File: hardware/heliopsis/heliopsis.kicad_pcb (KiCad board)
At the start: 2 copper layers, 70.7 x 53.3 mm, 311 parts, among them J1 NEIGHBOR1, J11 NEIGHBOR1, J12 NEIGHBOR2, J17 BONUS_ROW, J2 NEIGHBOR2, J7 BONUS_ROW, P1101 smd-proto-pad, P11010 smd-proto-pad, P11011 smd-proto-pad, P11012 smd-proto-pad, P11013 smd-proto-pad, P11014 smd-proto-pad, P11015 smd-proto-pad, P1102 smd-proto-pad, P1103 smd-proto-pad, P1104 smd-proto-pad, P1105 smd-proto-pad, P1106 smd-proto-pad, P1107 smd-proto-pad, P1108 smd-proto-pad, P1109 smd-proto-pad, P111 smd-proto-pad, P1110 smd-proto-pad, P1111 smd-proto-pad, P11110 smd-proto-pad, P11111 smd-proto-pad, P11112 smd-proto-pad, P11113 smd-proto-pad, P11114 smd-proto-pad, P11115 smd-proto-pad, P1112 smd-proto-pad, P1113 smd-proto-pad, P1114 smd-proto-pad, P1115 smd-proto-pad, P1116 smd-proto-pad, P1117 smd-proto-pad, P1118 smd-proto-pad, P1119 smd-proto-pad, P112 smd-proto-pad, P1121 smd-proto-pad, P11210 smd-proto-pad, P11211 smd-proto-pad, P11212 smd-proto-pad, P11213 smd-proto-pad, P11214 smd-proto-pad, P11215 smd-proto-pad, P1122 smd-proto-pad, P1123 smd-proto-pad, P1124 smd-proto-pad, P1125 smd-proto-pad, P1126 smd-proto-pad, P1127 smd-proto-pad, P1128 smd-proto-pad, P1129 smd-proto-pad, P113 smd-proto-pad, P1131 smd-proto-pad, P11310 smd-proto-pad, P11311 smd-proto-pad, P11312 smd-proto-pad, P11313 smd-proto-pad, P11314 smd-proto-pad, P11315 smd-proto-pad, P1132 smd-proto-pad, P1133 smd-proto-pad, P1134 smd-proto-pad, P1135 smd-proto-pad, P1136 smd-proto-pad, P1137 smd-proto-pad, P1138 smd-proto-pad, P1139 smd-proto-pad, P114 smd-proto-pad, P1141 smd-proto-pad, P11410 smd-proto-pad, P11411 smd-proto-pad, P11412 smd-proto-pad, P11413 smd-proto-pad, P11414 smd-proto-pad, P11415 smd-proto-pad, P1142 smd-proto-pad, P1143 smd-proto-pad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

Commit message: Update date for this version
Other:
- board text added: "2 September 2016"
- board text removed: "18 August 2016"
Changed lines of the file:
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@@
   (gr_line (start 177.9016 92.3544) (end 177.8508 94.0054) (angle 90) (layer Edge.Cuts) (width 0.15))
   (gr_line (start 177.9524 90.5002) (end 177.9016 92.3544) (angle 90) (layer Edge.Cuts) (width 0.15))
-  (gr_text "18 August 2016" (at 153.416 114.681) (layer F.SilkS)
+  (gr_text "2 September 2016" (at 153.416 114.681) (layer F.SilkS)
     (effects (font (size 0.762 0.5715) (thickness 0.1143)))
   )

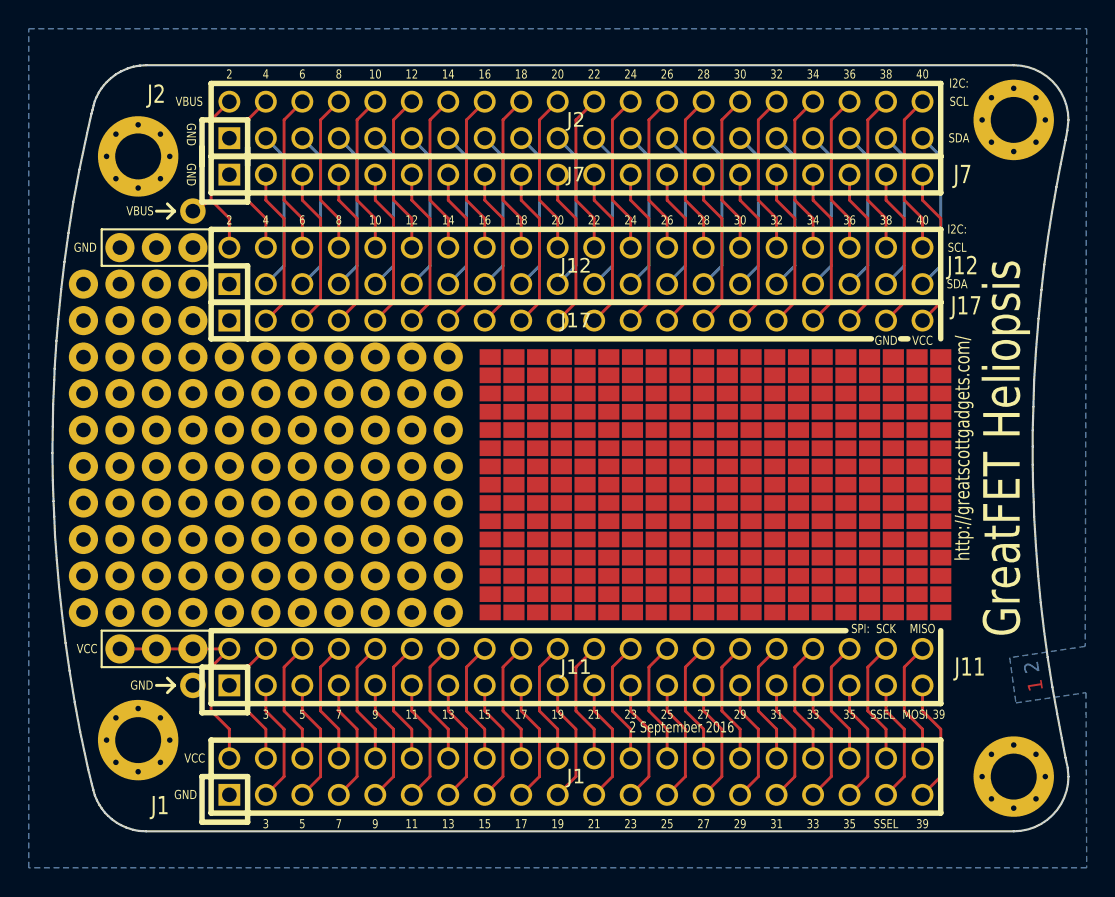
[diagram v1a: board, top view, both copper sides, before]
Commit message: Make power traces wider
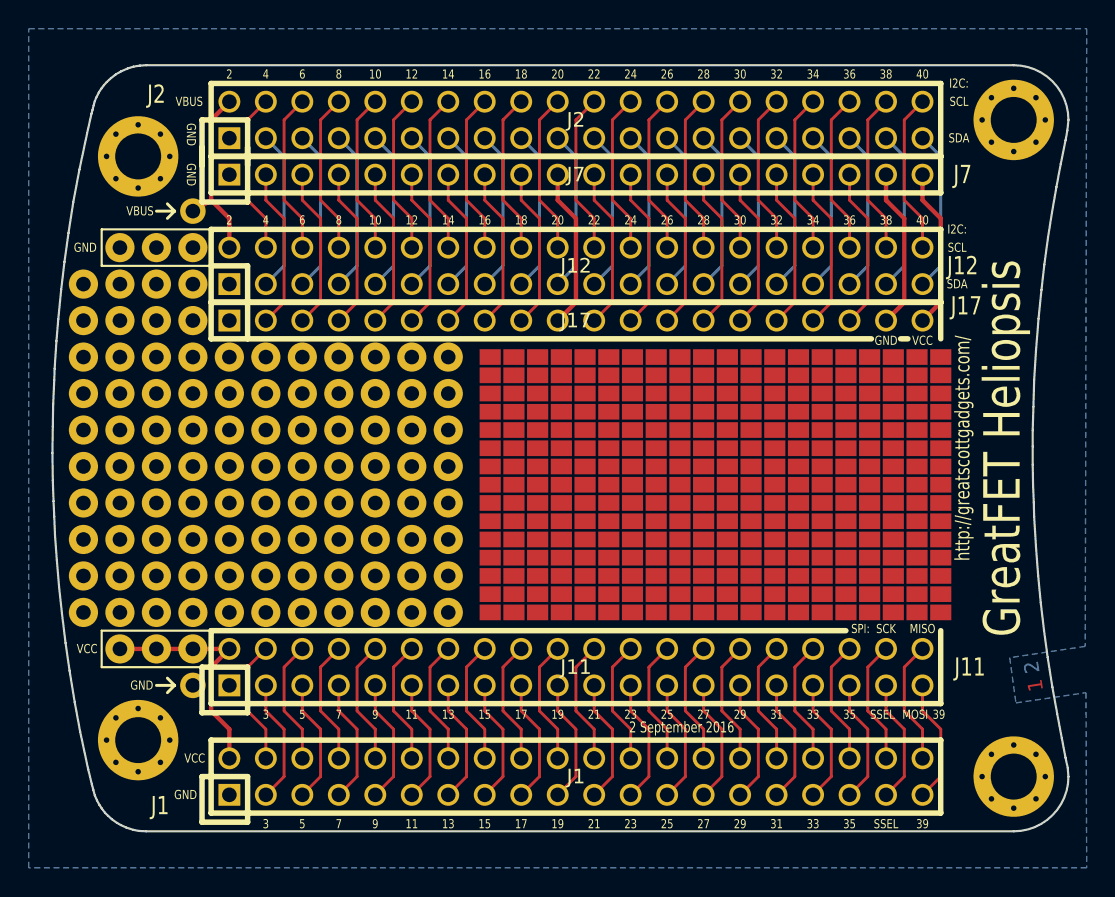
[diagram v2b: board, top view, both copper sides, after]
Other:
- net class Power added: clearance 0.1524, trace_width 0.3048, via_dia 0.762, via_drill 0.3302
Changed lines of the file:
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@@
-(kicad_pcb (version 4) (host pcbnew 4.0.2-stable)
+(kicad_pcb (version 4) (host pcbnew 4.0.4-stable)
   (general
     (links 149)
@@
   )
   (setup
-    (last_trace_width 0.2032)
+    (last_trace_width 0.3048)
     (user_trace_width 0.3048)
     (user_trace_width 0.508)
@@
     (visible_elements FFFFF77F)
     (pcbplotparams
-      (layerselection 0x010e8_80000001)
+      (layerselection 0x010f0_80000001)
       (usegerberextensions false)
       (excludeedgelayer true)
@@
     (add_net /RTC_ALARM)
     (add_net /VBAT)
-    (add_net /VBUS)
     (add_net /WAKEUP0)
+  )
+  (net_class Power ""
+    (clearance 0.1524)
+    (trace_width 0.3048)
+    (via_dia 0.762)
+    (via_drill 0.3302)
+    (uvia_dia 0.508)
+    (uvia_drill 0.2032)
+    (add_net /VBUS)
     (add_net GND)
     (add_net VCC)
@@
   (gr_line (start 176.53 121.92) (end 116.1288 121.92) (angle 90) (layer Edge.Cuts) (width 0.15))
   (gr_line (start 116.1288 68.58) (end 176.53 68.58) (angle 90) (layer Edge.Cuts) (width 0.15))
-  (segment (start 167.64 77.978) (end 167.64 76.2) (width 0.2032) (layer F.Cu) (net 1) (status 20))
-  (segment (start 168.91 79.248) (end 167.64 77.978) (width 0.2032) (layer F.Cu) (net 1))
-  (segment (start 168.91 85.09) (end 168.91 79.248) (width 0.2032) (layer F.Cu) (net 1))
-  (segment (start 167.64 86.36) (end 168.91 85.09) (width 0.2032) (layer F.Cu) (net 1) (status 10))
-  (segment (start 146.05 79.248) (end 144.78 77.978) (width 0.2032) (layer F.Cu) (net 1))
-  (segment (start 144.78 77.978) (end 144.78 76.2) (width 0.2032) (layer F.Cu) (net 1) (status 20))
-  (segment (start 146.05 85.09) (end 146.05 79.248) (width 0.2032) (layer F.Cu) (net 1))
-  (segment (start 144.78 86.36) (end 146.05 85.09) (width 0.2032) (layer F.Cu) (net 1) (status 10))
-  (segment (start 116.84 109.22) (end 114.3 109.22) (width 0.2032) (layer F.Cu) (net 2))
-  (segment (start 119.38 109.22) (end 116.84 109.22) (width 0.2032) (layer F.Cu) (net 2))
-  (segment (start 121.92 109.22) (end 119.38 109.22) (width 0.2032) (layer F.Cu) (net 2))
-  (segment (start 170.18 77.978) (end 170.18 76.2) (width 0.2032) (layer F.Cu) (net 2) (status 20))
-  (segment (start 171.45 79.248) (end 170.18 77.978) (width 0.2032) (layer F.Cu) (net 2))
-  (segment (start 171.45 85.09) (end 171.45 79.248) (width 0.2032) (layer F.Cu) (net 2))
-  (segment (start 170.18 86.36) (end 171.45 85.09) (width 0.2032) (layer F.Cu) (net 2) (status 10))
-  (segment (start 120.65 113.538) (end 120.65 110.49) (width 0.2032) (layer F.Cu) (net 2))
-  (segment (start 120.65 110.49) (end 121.92 109.22) (width 0.2032) (layer F.Cu) (net 2) (status 20))
-  (segment (start 121.92 114.808) (end 120.65 113.538) (width 0.2032) (layer F.Cu) (net 2))
-  (segment (start 121.92 116.84) (end 121.92 114.808) (width 0.2032) (layer F.Cu) (net 2) (status 10))
-  (segment (start 119.38 78.74) (end 120.65 77.978) (width 0.2032) (layer F.Cu) (net 3))
-  (segment (start 121.92 81.28) (end 121.92 79.248) (width 0.2032) (layer F.Cu) (net 3) (status 10))
-  (segment (start 121.92 79.248) (end 120.65 77.978) (width 0.2032) (layer F.Cu) (net 3))
-  (segment (start 120.65 77.978) (end 120.65 72.39) (width 0.2032) (layer F.Cu) (net 3))
-  (segment (start 120.65 72.39) (end 121.92 71.12) (width 0.2032) (layer F.Cu) (net 3) (status 20))
+  (segment (start 167.64 77.978) (end 167.64 76.2) (width 0.3048) (layer F.Cu) (net 1) (status 20))
+  (segment (start 168.91 79.248) (end 167.64 77.978) (width 0.3048) (layer F.Cu) (net 1))
+  (segment (start 168.91 85.09) (end 168.91 79.248) (width 0.3048) (layer F.Cu) (net 1))
+  (segment (start 167.64 86.36) (end 168.91 85.09) (width 0.3048) (layer F.Cu) (net 1) (status 10))
+  (segment (start 146.05 79.248) (end 144.78 77.978) (width 0.3048) (layer F.Cu) (net 1))
+  (segment (start 144.78 86.36) (end 146.05 85.09) (width 0.3048) (layer F.Cu) (net 1) (status 10))
+  (segment (start 146.05 85.09) (end 146.05 79.248) (width 0.3048) (layer F.Cu) (net 1))
+  (segment (start 144.78 77.978) (end 144.78 76.2) (width 0.3048) (layer F.Cu) (net 1) (status 20))
+  (segment (start 116.84 109.22) (end 114.3 109.22) (width 0.3048) (layer F.Cu) (net 2))
+  (segment (start 119.38 109.22) (end 116.84 109.22) (width 0.3048) (layer F.Cu) (net 2))
+  (segment (start 121.92 109.22) (end 119.38 109.22) (width 0.3048) (layer F.Cu) (net 2))
+  (segment (start 170.18 77.978) (end 170.18 76.2) (width 0.3048) (layer F.Cu) (net 2) (status 20))
+  (segment (start 170.18 86.36) (end 171.45 85.09) (width 0.3048) (layer F.Cu) (net 2) (status 10))
+  (segment (start 171.45 85.09) (end 171.45 79.248) (width 0.3048) (layer F.Cu) (net 2))
+  (segment (start 171.45 79.248) (end 170.18 77.978) (width 0.3048) (layer F.Cu) (net 2))
+  (segment (start 120.65 113.538) (end 120.65 110.49) (width 0.3048) (layer F.Cu) (net 2))
+  (segment (start 121.92 116.84) (end 121.92 114.808) (width 0.3048) (layer F.Cu) (net 2) (status 10))
+  (segment (start 121.92 114.808) (end 120.65 113.538) (width 0.3048) (layer F.Cu) (net 2))
+  (segment (start 120.65 110.49) (end 121.92 109.22) (width 0.3048) (layer F.Cu) (net 2) (status 20))
+  (segment (start 119.38 78.74) (end 120.65 77.978) (width 0.3048) (layer F.Cu) (net 3))
+  (segment (start 121.92 81.28) (end 121.92 79.248) (width 0.3048) (layer F.Cu) (net 3) (status 10))
+  (segment (start 121.92 79.248) (end 120.65 77.978) (width 0.3048) (layer F.Cu) (net 3))
+  (segment (start 120.65 77.978) (end 120.65 72.39) (width 0.3048) (layer F.Cu) (net 3))
+  (segment (start 120.65 72.39) (end 121.92 71.12) (width 0.3048) (layer F.Cu) (net 3) (status 20))
   (segment (start 124.46 113.538) (end 124.46 111.76) (width 0.2032) (layer F.Cu) (net 4) (status 20))
   (segment (start 125.73 114.808) (end 124.46 113.538) (width 0.2032) (layer F.Cu) (net 4))

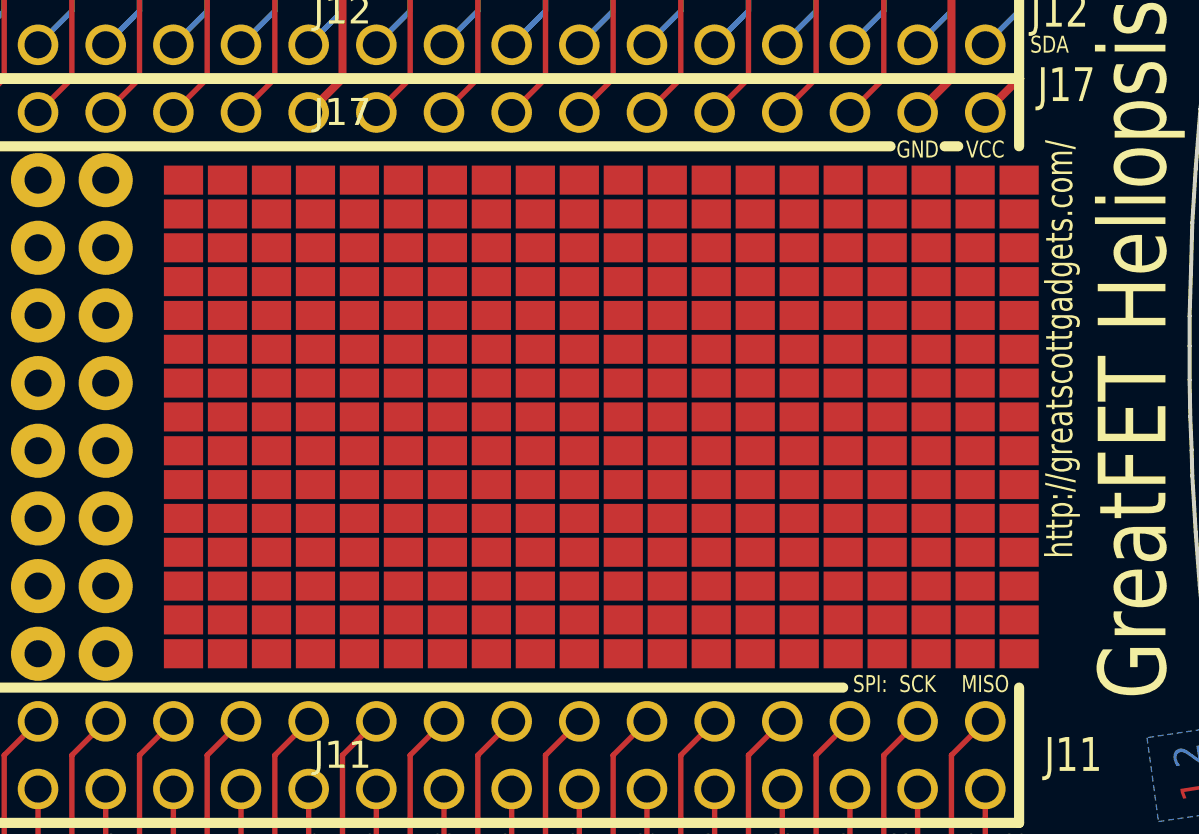
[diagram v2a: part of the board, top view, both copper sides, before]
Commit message: Add nonplated through holes for SMD prototyping
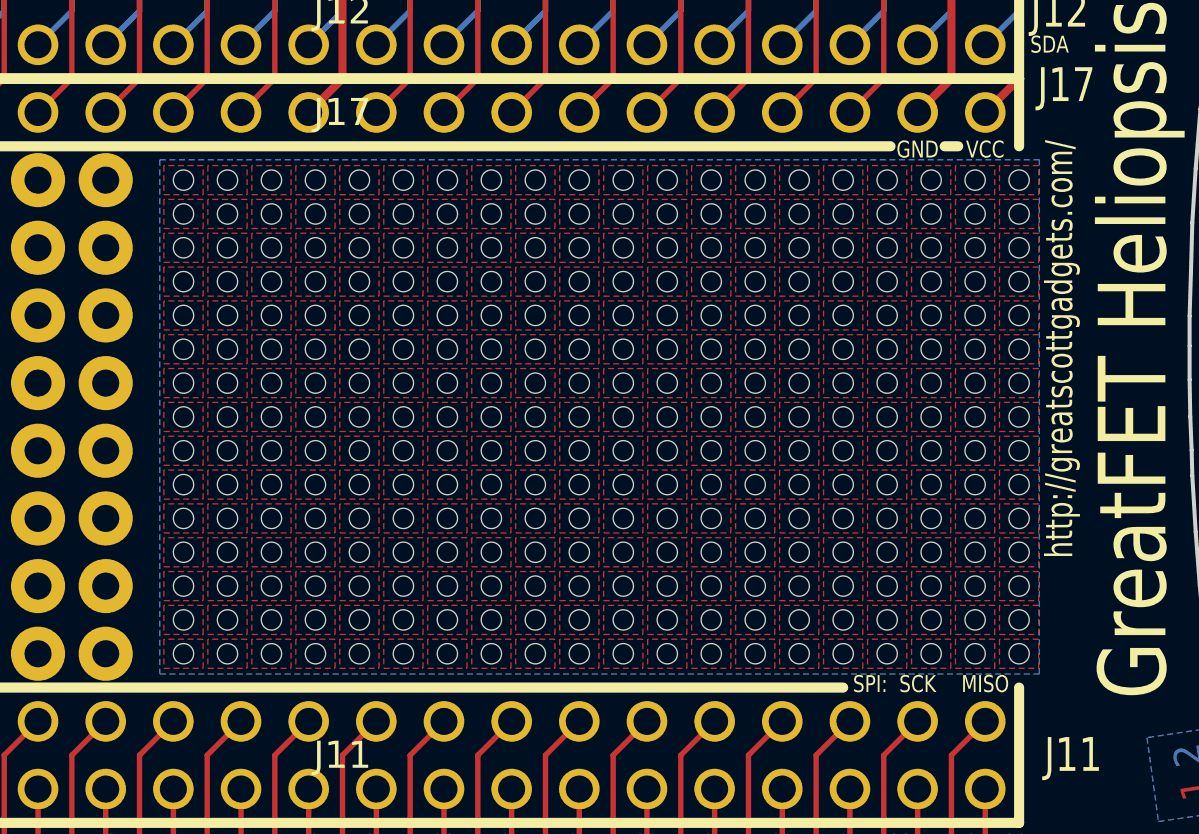
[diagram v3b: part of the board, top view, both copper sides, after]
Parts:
- removed P1101, P11010, P11011, P11012, P11013, P11014, P11015, P1102, P1103, P1104, P1105, P1106, P1107, P1108, P1109, P111, P1110, P1111 (x2), P11110, P11111, P11112, P11113, P11114, P11115, P1112 (x2), P1113 (x2), P1114 (x2), P1115 (x2), P1116, P1117, P1118, P1119, P112, P1121, P11210, P11211, P11212, P11213, P11214, P11215, P1122, P1123, P1124, P1125, P1126, P1127, P1128, P1129, P113, P1131, P11310, P11311, P11312, P11313, P11314, P11315, P1132, P1133, P1134, P1135, P1136, P1137, P1138, P1139, P114, P1141, P11410, P11411, P11412, P11413, P11414, P11415, P1142, P1143, P1144, P1145, P1146, P1147, P1148, P1149, P115, P1151, P11510, P11511, P11512, P11513, P11514, P11515, P1152, P1153, P1154, P1155, P1156, P1157, P1158, P1159, P116, P1161, P11610, P11611, P11612, P11613, P11614, P11615, P1162, P1163, P1164, P1165, P1166, P1167, P1168, P1169, P117, P1171, P11710, P11711, P11712, P11713, P11714, P11715, P1172, P1173, P1174, P1175, P1176, P1177, P1178, P1179, P118, P1181, P11810, P11811, P11812, P11813, P11814, P11815, P1182, P1183, P1184, P1185, P1186, P1187, P1188, P1189, P119, P1191, P11910, P11911, P11912, P11913, P11914, P11915, P1192, P1193, P1194, P1195, P1196, P1197, P1198, P1199, P1201, P12010, P12011, P12012, P12013, P12014, P12015, P1202, P1203, P1204, P1205, P1206, P1207, P1208, P1209, P121, P1210, P1211, P1212, P1213, P1214, P1215, P122, P123, P124, P125, P126, P127, P128, P129, P131, P1310, P1311, P1312, P1313, P1314, P1315, P132, P133, P134, P135, P136, P137, P138, P139, P141, P1410, P1411, P1412, P1413, P1414, P1415, P142, P143, P144, P145, P146, P147, P148, P149, P151, P1510, P1511, P1512, P1513, P1514, P1515, P152, P153, P154, P155, P156, P157, P158, P159, P161, P1610, P1611, P1612, P1613, P1614, P1615, P162, P163, P164, P165, P166, P167, P168, P169, P171, P1710, P1711, P1712, P1713, P1714, P1715, P172, P173, P174, P175, P176, P177, P178, P179, P181, P1810, P1811, P1812, P1813, P1814, P1815, P182, P183, P184, P185, P186, P187, P188, P189, P191, P1910, P1911, P1912, P1913, P1914, P1915, P192, P193, P194, P195, P196, P197, P198, P199: smd-proto-pad, heliopsis-modules:smd-proto-pad
- added H1: smd-proto-hole, smd-proto-hole, F.Cu at (140.1, 106.7)
- added H1: smd-proto-hole, smd-proto-hole, F.Cu at (154.9, 106.7)
- added H1: smd-proto-hole, smd-proto-hole, F.Cu at (171.4, 101.6)
- added H1: smd-proto-hole, smd-proto-hole, F.Cu at (140.1, 100.3)
- added H1: smd-proto-hole, smd-proto-hole, F.Cu at (141.7, 100.3)
- added H1: smd-proto-hole, smd-proto-hole, F.Cu at (143.4, 100.3)
- added H1: smd-proto-hole, smd-proto-hole, F.Cu at (145.0, 100.3)
- added H1: smd-proto-hole, smd-proto-hole, F.Cu at (146.7, 100.3)
- added H1: smd-proto-hole, smd-proto-hole, F.Cu at (148.3, 100.3)
- added H1: smd-proto-hole, smd-proto-hole, F.Cu at (150.0, 100.3)
- added H1: smd-proto-hole, smd-proto-hole, F.Cu at (151.6, 100.3)
- added H1: smd-proto-hole, smd-proto-hole, F.Cu at (153.3, 100.3)
- added H1: smd-proto-hole, smd-proto-hole, F.Cu at (156.6, 106.7)
- added H1: smd-proto-hole, smd-proto-hole, F.Cu at (154.9, 100.3)
- added H1: smd-proto-hole, smd-proto-hole, F.Cu at (156.6, 100.3)
- added H1: smd-proto-hole, smd-proto-hole, F.Cu at (158.2, 100.3)
- added H1: smd-proto-hole, smd-proto-hole, F.Cu at (159.9, 100.3)
- added H1: smd-proto-hole, smd-proto-hole, F.Cu at (161.5, 100.3)
- added H1: smd-proto-hole, smd-proto-hole, F.Cu at (163.2, 100.3)
- added H1: smd-proto-hole, smd-proto-hole, F.Cu at (164.8, 100.3)
- added H1: smd-proto-hole, smd-proto-hole, F.Cu at (166.5, 100.3)
- added H1: smd-proto-hole, smd-proto-hole, F.Cu at (168.1, 100.3)
- added H1: smd-proto-hole, smd-proto-hole, F.Cu at (169.8, 100.3)
- added H1: smd-proto-hole, smd-proto-hole, F.Cu at (158.2, 106.7)
- added H1: smd-proto-hole, smd-proto-hole, F.Cu at (171.4, 100.3)
- added H1: smd-proto-hole, smd-proto-hole, F.Cu at (140.1, 99.1)
- added H1: smd-proto-hole, smd-proto-hole, F.Cu at (141.7, 99.1)
- added H1: smd-proto-hole, smd-proto-hole, F.Cu at (143.4, 99.1)
- added H1: smd-proto-hole, smd-proto-hole, F.Cu at (145.0, 99.1)
- added H1: smd-proto-hole, smd-proto-hole, F.Cu at (146.7, 99.1)
- added H1: smd-proto-hole, smd-proto-hole, F.Cu at (148.3, 99.1)
- added H1: smd-proto-hole, smd-proto-hole, F.Cu at (150.0, 99.1)
- added H1: smd-proto-hole, smd-proto-hole, F.Cu at (151.6, 99.1)
- added H1: smd-proto-hole, smd-proto-hole, F.Cu at (153.3, 99.1)
- added H1: smd-proto-hole, smd-proto-hole, F.Cu at (159.9, 106.7)
- added H1: smd-proto-hole, smd-proto-hole, F.Cu at (154.9, 99.1)
- added H1: smd-proto-hole, smd-proto-hole, F.Cu at (156.6, 99.1)
- added H1: smd-proto-hole, smd-proto-hole, F.Cu at (158.2, 99.1)
- added H1: smd-proto-hole, smd-proto-hole, F.Cu at (159.9, 99.1)
- added H1: smd-proto-hole, smd-proto-hole, F.Cu at (161.5, 99.1)
- added H1: smd-proto-hole, smd-proto-hole, F.Cu at (163.2, 99.1)
- added H1: smd-proto-hole, smd-proto-hole, F.Cu at (164.8, 99.1)
- added H1: smd-proto-hole, smd-proto-hole, F.Cu at (166.5, 99.1)
- added H1: smd-proto-hole, smd-proto-hole, F.Cu at (168.1, 99.1)
- added H1: smd-proto-hole, smd-proto-hole, F.Cu at (169.8, 99.1)
- added H1: smd-proto-hole, smd-proto-hole, F.Cu at (161.5, 106.7)
- added H1: smd-proto-hole, smd-proto-hole, F.Cu at (171.4, 99.1)
- added H1: smd-proto-hole, smd-proto-hole, F.Cu at (140.1, 97.8)
- added H1: smd-proto-hole, smd-proto-hole, F.Cu at (141.7, 97.8)
- added H1: smd-proto-hole, smd-proto-hole, F.Cu at (143.4, 97.8)
- added H1: smd-proto-hole, smd-proto-hole, F.Cu at (145.0, 97.8)
- added H1: smd-proto-hole, smd-proto-hole, F.Cu at (146.7, 97.8)
- added H1: smd-proto-hole, smd-proto-hole, F.Cu at (148.3, 97.8)
- added H1: smd-proto-hole, smd-proto-hole, F.Cu at (150.0, 97.8)
- added H1: smd-proto-hole, smd-proto-hole, F.Cu at (151.6, 97.8)
- added H1: smd-proto-hole, smd-proto-hole, F.Cu at (153.3, 97.8)
- added H1: smd-proto-hole, smd-proto-hole, F.Cu at (163.2, 106.7)
- added H1: smd-proto-hole, smd-proto-hole, F.Cu at (154.9, 97.8)
- added H1: smd-proto-hole, smd-proto-hole, F.Cu at (156.6, 97.8)
- added H1: smd-proto-hole, smd-proto-hole, F.Cu at (158.2, 97.8)
- added H1: smd-proto-hole, smd-proto-hole, F.Cu at (159.9, 97.8)
- added H1: smd-proto-hole, smd-proto-hole, F.Cu at (161.5, 97.8)
- added H1: smd-proto-hole, smd-proto-hole, F.Cu at (163.2, 97.8)
- added H1: smd-proto-hole, smd-proto-hole, F.Cu at (164.8, 97.8)
- added H1: smd-proto-hole, smd-proto-hole, F.Cu at (166.5, 97.8)
- added H1: smd-proto-hole, smd-proto-hole, F.Cu at (168.1, 97.8)
- added H1: smd-proto-hole, smd-proto-hole, F.Cu at (169.8, 97.8)
- added H1: smd-proto-hole, smd-proto-hole, F.Cu at (164.8, 106.7)
- added H1: smd-proto-hole, smd-proto-hole, F.Cu at (171.4, 97.8)
- added H1: smd-proto-hole, smd-proto-hole, F.Cu at (140.1, 96.5)
- added H1: smd-proto-hole, smd-proto-hole, F.Cu at (141.7, 96.5)
- added H1: smd-proto-hole, smd-proto-hole, F.Cu at (143.4, 96.5)
- added H1: smd-proto-hole, smd-proto-hole, F.Cu at (145.0, 96.5)
- added H1: smd-proto-hole, smd-proto-hole, F.Cu at (146.7, 96.5)
- added H1: smd-proto-hole, smd-proto-hole, F.Cu at (148.3, 96.5)
- added H1: smd-proto-hole, smd-proto-hole, F.Cu at (150.0, 96.5)
- added H1: smd-proto-hole, smd-proto-hole, F.Cu at (151.6, 96.5)
- added H1: smd-proto-hole, smd-proto-hole, F.Cu at (153.3, 96.5)
- added H1: smd-proto-hole, smd-proto-hole, F.Cu at (166.5, 106.7)
- added H1: smd-proto-hole, smd-proto-hole, F.Cu at (154.9, 96.5)
- added H1: smd-proto-hole, smd-proto-hole, F.Cu at (156.6, 96.5)
- added H1: smd-proto-hole, smd-proto-hole, F.Cu at (158.2, 96.5)
- added H1: smd-proto-hole, smd-proto-hole, F.Cu at (159.9, 96.5)
- added H1: smd-proto-hole, smd-proto-hole, F.Cu at (161.5, 96.5)
- added H1: smd-proto-hole, smd-proto-hole, F.Cu at (163.2, 96.5)
- added H1: smd-proto-hole, smd-proto-hole, F.Cu at (164.8, 96.5)
- added H1: smd-proto-hole, smd-proto-hole, F.Cu at (166.5, 96.5)
- added H1: smd-proto-hole, smd-proto-hole, F.Cu at (168.1, 96.5)
- added H1: smd-proto-hole, smd-proto-hole, F.Cu at (169.8, 96.5)
- added H1: smd-proto-hole, smd-proto-hole, F.Cu at (168.1, 106.7)
- added H1: smd-proto-hole, smd-proto-hole, F.Cu at (171.4, 96.5)
- added H1: smd-proto-hole, smd-proto-hole, F.Cu at (140.1, 95.2)
- added H1: smd-proto-hole, smd-proto-hole, F.Cu at (141.7, 95.2)
- added H1: smd-proto-hole, smd-proto-hole, F.Cu at (143.4, 95.2)
- added H1: smd-proto-hole, smd-proto-hole, F.Cu at (145.0, 95.2)
- added H1: smd-proto-hole, smd-proto-hole, F.Cu at (146.7, 95.2)
- added H1: smd-proto-hole, smd-proto-hole, F.Cu at (148.3, 95.2)
- added H1: smd-proto-hole, smd-proto-hole, F.Cu at (150.0, 95.2)
- added H1: smd-proto-hole, smd-proto-hole, F.Cu at (151.6, 95.2)
- added H1: smd-proto-hole, smd-proto-hole, F.Cu at (153.3, 95.2)
- added H1: smd-proto-hole, smd-proto-hole, F.Cu at (169.8, 106.7)
- added H1: smd-proto-hole, smd-proto-hole, F.Cu at (154.9, 95.2)
- added H1: smd-proto-hole, smd-proto-hole, F.Cu at (156.6, 95.2)
- added H1: smd-proto-hole, smd-proto-hole, F.Cu at (158.2, 95.2)
- added H1: smd-proto-hole, smd-proto-hole, F.Cu at (159.9, 95.2)
- added H1: smd-proto-hole, smd-proto-hole, F.Cu at (161.5, 95.2)
- added H1: smd-proto-hole, smd-proto-hole, F.Cu at (163.2, 95.2)
- added H1: smd-proto-hole, smd-proto-hole, F.Cu at (164.8, 95.2)
- added H1: smd-proto-hole, smd-proto-hole, F.Cu at (166.5, 95.2)
- added H1: smd-proto-hole, smd-proto-hole, F.Cu at (168.1, 95.2)
- added H1: smd-proto-hole, smd-proto-hole, F.Cu at (169.8, 95.2)
- added H1: smd-proto-hole, smd-proto-hole, F.Cu at (141.7, 106.7)
- added H1: smd-proto-hole, smd-proto-hole, F.Cu at (171.4, 106.7)
- added H1: smd-proto-hole, smd-proto-hole, F.Cu at (171.4, 95.2)
- added H1: smd-proto-hole, smd-proto-hole, F.Cu at (140.1, 94.0)
- added H1: smd-proto-hole, smd-proto-hole, F.Cu at (141.7, 94.0)
- added H1: smd-proto-hole, smd-proto-hole, F.Cu at (143.4, 94.0)
- added H1: smd-proto-hole, smd-proto-hole, F.Cu at (145.0, 94.0)
- added H1: smd-proto-hole, smd-proto-hole, F.Cu at (146.7, 94.0)
- added H1: smd-proto-hole, smd-proto-hole, F.Cu at (148.3, 94.0)
- added H1: smd-proto-hole, smd-proto-hole, F.Cu at (150.0, 94.0)
- added H1: smd-proto-hole, smd-proto-hole, F.Cu at (151.6, 94.0)
- added H1: smd-proto-hole, smd-proto-hole, F.Cu at (153.3, 94.0)
- added H1: smd-proto-hole, smd-proto-hole, F.Cu at (140.1, 105.4)
- added H1: smd-proto-hole, smd-proto-hole, F.Cu at (154.9, 94.0)
- added H1: smd-proto-hole, smd-proto-hole, F.Cu at (156.6, 94.0)
- added H1: smd-proto-hole, smd-proto-hole, F.Cu at (158.2, 94.0)
- added H1: smd-proto-hole, smd-proto-hole, F.Cu at (159.9, 94.0)
- added H1: smd-proto-hole, smd-proto-hole, F.Cu at (161.5, 94.0)
- added H1: smd-proto-hole, smd-proto-hole, F.Cu at (163.2, 94.0)
- added H1: smd-proto-hole, smd-proto-hole, F.Cu at (164.8, 94.0)
- added H1: smd-proto-hole, smd-proto-hole, F.Cu at (166.5, 94.0)
- added H1: smd-proto-hole, smd-proto-hole, F.Cu at (168.1, 94.0)
- added H1: smd-proto-hole, smd-proto-hole, F.Cu at (169.8, 94.0)
- added H1: smd-proto-hole, smd-proto-hole, F.Cu at (141.7, 105.4)
- added H1: smd-proto-hole, smd-proto-hole, F.Cu at (171.4, 94.0)
- added H1: smd-proto-hole, smd-proto-hole, F.Cu at (140.1, 92.7)
- added H1: smd-proto-hole, smd-proto-hole, F.Cu at (141.7, 92.7)
- added H1: smd-proto-hole, smd-proto-hole, F.Cu at (143.4, 92.7)
- added H1: smd-proto-hole, smd-proto-hole, F.Cu at (145.0, 92.7)
- added H1: smd-proto-hole, smd-proto-hole, F.Cu at (146.7, 92.7)
- added H1: smd-proto-hole, smd-proto-hole, F.Cu at (148.3, 92.7)
- added H1: smd-proto-hole, smd-proto-hole, F.Cu at (150.0, 92.7)
- added H1: smd-proto-hole, smd-proto-hole, F.Cu at (151.6, 92.7)
- added H1: smd-proto-hole, smd-proto-hole, F.Cu at (153.3, 92.7)
- added H1: smd-proto-hole, smd-proto-hole, F.Cu at (143.4, 105.4)
- added H1: smd-proto-hole, smd-proto-hole, F.Cu at (154.9, 92.7)
- added H1: smd-proto-hole, smd-proto-hole, F.Cu at (156.6, 92.7)
- added H1: smd-proto-hole, smd-proto-hole, F.Cu at (158.2, 92.7)
- added H1: smd-proto-hole, smd-proto-hole, F.Cu at (159.9, 92.7)
- added H1: smd-proto-hole, smd-proto-hole, F.Cu at (161.5, 92.7)
- added H1: smd-proto-hole, smd-proto-hole, F.Cu at (163.2, 92.7)
- added H1: smd-proto-hole, smd-proto-hole, F.Cu at (164.8, 92.7)
- added H1: smd-proto-hole, smd-proto-hole, F.Cu at (166.5, 92.7)
- added H1: smd-proto-hole, smd-proto-hole, F.Cu at (168.1, 92.7)
- added H1: smd-proto-hole, smd-proto-hole, F.Cu at (169.8, 92.7)
- added H1: smd-proto-hole, smd-proto-hole, F.Cu at (145.0, 105.4)
- added H1: smd-proto-hole, smd-proto-hole, F.Cu at (171.4, 92.7)
- added H1: smd-proto-hole, smd-proto-hole, F.Cu at (140.1, 91.4)
- added H1: smd-proto-hole, smd-proto-hole, F.Cu at (141.7, 91.4)
- added H1: smd-proto-hole, smd-proto-hole, F.Cu at (143.4, 91.4)
- added H1: smd-proto-hole, smd-proto-hole, F.Cu at (145.0, 91.4)
- added H1: smd-proto-hole, smd-proto-hole, F.Cu at (146.7, 91.4)
- added H1: smd-proto-hole, smd-proto-hole, F.Cu at (148.3, 91.4)
- added H1: smd-proto-hole, smd-proto-hole, F.Cu at (150.0, 91.4)
- added H1: smd-proto-hole, smd-proto-hole, F.Cu at (151.6, 91.4)
- added H1: smd-proto-hole, smd-proto-hole, F.Cu at (153.3, 91.4)
- added H1: smd-proto-hole, smd-proto-hole, F.Cu at (146.7, 105.4)
- added H1: smd-proto-hole, smd-proto-hole, F.Cu at (154.9, 91.4)
- added H1: smd-proto-hole, smd-proto-hole, F.Cu at (156.6, 91.4)
- added H1: smd-proto-hole, smd-proto-hole, F.Cu at (158.2, 91.4)
- added H1: smd-proto-hole, smd-proto-hole, F.Cu at (159.9, 91.4)
- added H1: smd-proto-hole, smd-proto-hole, F.Cu at (161.5, 91.4)
- added H1: smd-proto-hole, smd-proto-hole, F.Cu at (163.2, 91.4)
- added H1: smd-proto-hole, smd-proto-hole, F.Cu at (164.8, 91.4)
- added H1: smd-proto-hole, smd-proto-hole, F.Cu at (166.5, 91.4)
- added H1: smd-proto-hole, smd-proto-hole, F.Cu at (168.1, 91.4)
- added H1: smd-proto-hole, smd-proto-hole, F.Cu at (169.8, 91.4)
- added H1: smd-proto-hole, smd-proto-hole, F.Cu at (148.3, 105.4)
- added H1: smd-proto-hole, smd-proto-hole, F.Cu at (171.4, 91.4)
- added H1: smd-proto-hole, smd-proto-hole, F.Cu at (140.1, 90.2)
- added H1: smd-proto-hole, smd-proto-hole, F.Cu at (141.7, 90.2)
- added H1: smd-proto-hole, smd-proto-hole, F.Cu at (143.4, 90.2)
- added H1: smd-proto-hole, smd-proto-hole, F.Cu at (145.0, 90.2)
- added H1: smd-proto-hole, smd-proto-hole, F.Cu at (146.7, 90.2)
- added H1: smd-proto-hole, smd-proto-hole, F.Cu at (148.3, 90.2)
- added H1: smd-proto-hole, smd-proto-hole, F.Cu at (150.0, 90.2)
- added H1: smd-proto-hole, smd-proto-hole, F.Cu at (151.6, 90.2)
- added H1: smd-proto-hole, smd-proto-hole, F.Cu at (153.3, 90.2)
- added H1: smd-proto-hole, smd-proto-hole, F.Cu at (150.0, 105.4)
- added H1: smd-proto-hole, smd-proto-hole, F.Cu at (154.9, 90.2)
- added H1: smd-proto-hole, smd-proto-hole, F.Cu at (156.6, 90.2)
- added H1: smd-proto-hole, smd-proto-hole, F.Cu at (158.2, 90.2)
- added H1: smd-proto-hole, smd-proto-hole, F.Cu at (159.9, 90.2)
- added H1: smd-proto-hole, smd-proto-hole, F.Cu at (161.5, 90.2)
- added H1: smd-proto-hole, smd-proto-hole, F.Cu at (163.2, 90.2)
- added H1: smd-proto-hole, smd-proto-hole, F.Cu at (164.8, 90.2)
- added H1: smd-proto-hole, smd-proto-hole, F.Cu at (166.5, 90.2)
- added H1: smd-proto-hole, smd-proto-hole, F.Cu at (168.1, 90.2)
- added H1: smd-proto-hole, smd-proto-hole, F.Cu at (169.8, 90.2)
- added H1: smd-proto-hole, smd-proto-hole, F.Cu at (151.6, 105.4)
- added H1: smd-proto-hole, smd-proto-hole, F.Cu at (171.4, 90.2)
- added H1: smd-proto-hole, smd-proto-hole, F.Cu at (140.1, 88.9)
- added H1: smd-proto-hole, smd-proto-hole, F.Cu at (141.7, 88.9)
- added H1: smd-proto-hole, smd-proto-hole, F.Cu at (143.4, 88.9)
- added H1: smd-proto-hole, smd-proto-hole, F.Cu at (145.0, 88.9)
- added H1: smd-proto-hole, smd-proto-hole, F.Cu at (146.7, 88.9)
- added H1: smd-proto-hole, smd-proto-hole, F.Cu at (148.3, 88.9)
- added H1: smd-proto-hole, smd-proto-hole, F.Cu at (150.0, 88.9)
- added H1: smd-proto-hole, smd-proto-hole, F.Cu at (151.6, 88.9)
- added H1: smd-proto-hole, smd-proto-hole, F.Cu at (153.3, 88.9)
- added H1: smd-proto-hole, smd-proto-hole, F.Cu at (153.3, 105.4)
- added H1: smd-proto-hole, smd-proto-hole, F.Cu at (154.9, 88.9)
- added H1: smd-proto-hole, smd-proto-hole, F.Cu at (156.6, 88.9)
- added H1: smd-proto-hole, smd-proto-hole, F.Cu at (158.2, 88.9)
- added H1: smd-proto-hole, smd-proto-hole, F.Cu at (159.9, 88.9)
- added H1: smd-proto-hole, smd-proto-hole, F.Cu at (161.5, 88.9)
- added H1: smd-proto-hole, smd-proto-hole, F.Cu at (163.2, 88.9)
- added H1: smd-proto-hole, smd-proto-hole, F.Cu at (164.8, 88.9)
- added H1: smd-proto-hole, smd-proto-hole, F.Cu at (166.5, 88.9)
- added H1: smd-proto-hole, smd-proto-hole, F.Cu at (168.1, 88.9)
- added H1: smd-proto-hole, smd-proto-hole, F.Cu at (169.8, 88.9)
- added H1: smd-proto-hole, smd-proto-hole, F.Cu at (143.4, 106.7)
- added H1: smd-proto-hole, smd-proto-hole, F.Cu at (154.9, 105.4)
- added H1: smd-proto-hole, smd-proto-hole, F.Cu at (171.4, 88.9)
- added H1: smd-proto-hole, smd-proto-hole, F.Cu at (156.6, 105.4)
- added H1: smd-proto-hole, smd-proto-hole, F.Cu at (158.2, 105.4)
- added H1: smd-proto-hole, smd-proto-hole, F.Cu at (159.9, 105.4)
- added H1: smd-proto-hole, smd-proto-hole, F.Cu at (161.5, 105.4)
- added H1: smd-proto-hole, smd-proto-hole, F.Cu at (163.2, 105.4)
- added H1: smd-proto-hole, smd-proto-hole, F.Cu at (164.8, 105.4)
- added H1: smd-proto-hole, smd-proto-hole, F.Cu at (166.5, 105.4)
- added H1: smd-proto-hole, smd-proto-hole, F.Cu at (168.1, 105.4)
- added H1: smd-proto-hole, smd-proto-hole, F.Cu at (169.8, 105.4)
- added H1: smd-proto-hole, smd-proto-hole, F.Cu at (145.0, 106.7)
- added H1: smd-proto-hole, smd-proto-hole, F.Cu at (171.4, 105.4)
- added H1: smd-proto-hole, smd-proto-hole, F.Cu at (140.1, 104.1)
- added H1: smd-proto-hole, smd-proto-hole, F.Cu at (141.7, 104.1)
- added H1: smd-proto-hole, smd-proto-hole, F.Cu at (143.4, 104.1)
- added H1: smd-proto-hole, smd-proto-hole, F.Cu at (145.0, 104.1)
- added H1: smd-proto-hole, smd-proto-hole, F.Cu at (146.7, 104.1)
- added H1: smd-proto-hole, smd-proto-hole, F.Cu at (148.3, 104.1)
- added H1: smd-proto-hole, smd-proto-hole, F.Cu at (150.0, 104.1)
- added H1: smd-proto-hole, smd-proto-hole, F.Cu at (151.6, 104.1)
- added H1: smd-proto-hole, smd-proto-hole, F.Cu at (153.3, 104.1)
- added H1: smd-proto-hole, smd-proto-hole, F.Cu at (146.7, 106.7)
- added H1: smd-proto-hole, smd-proto-hole, F.Cu at (154.9, 104.1)
- added H1: smd-proto-hole, smd-proto-hole, F.Cu at (156.6, 104.1)
- added H1: smd-proto-hole, smd-proto-hole, F.Cu at (158.2, 104.1)
- added H1: smd-proto-hole, smd-proto-hole, F.Cu at (159.9, 104.1)
- added H1: smd-proto-hole, smd-proto-hole, F.Cu at (161.5, 104.1)
- added H1: smd-proto-hole, smd-proto-hole, F.Cu at (163.2, 104.1)
- added H1: smd-proto-hole, smd-proto-hole, F.Cu at (164.8, 104.1)
- added H1: smd-proto-hole, smd-proto-hole, F.Cu at (166.5, 104.1)
- added H1: smd-proto-hole, smd-proto-hole, F.Cu at (168.1, 104.1)
- added H1: smd-proto-hole, smd-proto-hole, F.Cu at (169.8, 104.1)
- added H1: smd-proto-hole, smd-proto-hole, F.Cu at (148.3, 106.7)
- added H1: smd-proto-hole, smd-proto-hole, F.Cu at (171.4, 104.1)
- added H1: smd-proto-hole, smd-proto-hole, F.Cu at (140.1, 102.9)
- added H1: smd-proto-hole, smd-proto-hole, F.Cu at (141.7, 102.9)
- added H1: smd-proto-hole, smd-proto-hole, F.Cu at (143.4, 102.9)
- added H1: smd-proto-hole, smd-proto-hole, F.Cu at (145.0, 102.9)
- added H1: smd-proto-hole, smd-proto-hole, F.Cu at (146.7, 102.9)
- added H1: smd-proto-hole, smd-proto-hole, F.Cu at (148.3, 102.9)
- added H1: smd-proto-hole, smd-proto-hole, F.Cu at (150.0, 102.9)
- added H1: smd-proto-hole, smd-proto-hole, F.Cu at (151.6, 102.9)
- added H1: smd-proto-hole, smd-proto-hole, F.Cu at (153.3, 102.9)
- added H1: smd-proto-hole, smd-proto-hole, F.Cu at (150.0, 106.7)
- added H1: smd-proto-hole, smd-proto-hole, F.Cu at (154.9, 102.9)
- added H1: smd-proto-hole, smd-proto-hole, F.Cu at (156.6, 102.9)
- added H1: smd-proto-hole, smd-proto-hole, F.Cu at (158.2, 102.9)
- added H1: smd-proto-hole, smd-proto-hole, F.Cu at (159.9, 102.9)
- added H1: smd-proto-hole, smd-proto-hole, F.Cu at (161.5, 102.9)
- added H1: smd-proto-hole, smd-proto-hole, F.Cu at (163.2, 102.9)
- added H1: smd-proto-hole, smd-proto-hole, F.Cu at (164.8, 102.9)
- added H1: smd-proto-hole, smd-proto-hole, F.Cu at (166.5, 102.9)
- added H1: smd-proto-hole, smd-proto-hole, F.Cu at (168.1, 102.9)
- added H1: smd-proto-hole, smd-proto-hole, F.Cu at (169.8, 102.9)
- added H1: smd-proto-hole, smd-proto-hole, F.Cu at (151.6, 106.7)
- added H1: smd-proto-hole, smd-proto-hole, F.Cu at (171.4, 102.9)
- added H1: smd-proto-hole, smd-proto-hole, F.Cu at (140.1, 101.6)
- added H1: smd-proto-hole, smd-proto-hole, F.Cu at (141.7, 101.6)
- added H1: smd-proto-hole, smd-proto-hole, F.Cu at (143.4, 101.6)
- added H1: smd-proto-hole, smd-proto-hole, F.Cu at (145.0, 101.6)
- added H1: smd-proto-hole, smd-proto-hole, F.Cu at (146.7, 101.6)
- added H1: smd-proto-hole, smd-proto-hole, F.Cu at (148.3, 101.6)
- added H1: smd-proto-hole, smd-proto-hole, F.Cu at (150.0, 101.6)
- added H1: smd-proto-hole, smd-proto-hole, F.Cu at (151.6, 101.6)
- added H1: smd-proto-hole, smd-proto-hole, F.Cu at (153.3, 101.6)
- added H1: smd-proto-hole, smd-proto-hole, F.Cu at (153.3, 106.7)
- added H1: smd-proto-hole, smd-proto-hole, F.Cu at (154.9, 101.6)
- added H1: smd-proto-hole, smd-proto-hole, F.Cu at (156.6, 101.6)
- added H1: smd-proto-hole, smd-proto-hole, F.Cu at (158.2, 101.6)
- added H1: smd-proto-hole, smd-proto-hole, F.Cu at (159.9, 101.6)
- added H1: smd-proto-hole, smd-proto-hole, F.Cu at (161.5, 101.6)
- added H1: smd-proto-hole, smd-proto-hole, F.Cu at (163.2, 101.6)
- added H1: smd-proto-hole, smd-proto-hole, F.Cu at (164.8, 101.6)
- added H1: smd-proto-hole, smd-proto-hole, F.Cu at (166.5, 101.6)
- added H1: smd-proto-hole, smd-proto-hole, F.Cu at (168.1, 101.6)
- added H1: smd-proto-hole, smd-proto-hole, F.Cu at (169.8, 101.6)
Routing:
- added copper zone on B.Cu, net (none)
- added copper zone on F.Cu, net (none)
